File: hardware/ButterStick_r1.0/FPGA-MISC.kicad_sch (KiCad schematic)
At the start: 11 parts, among them U4 ECP5UM5G_85_CABGA381, X1 ASDMB

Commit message: hw.r1d0: Review complete, gerbers generated
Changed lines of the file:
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@@
 (kicad_sch (version 20200618) (host eeschema "5.99.0-unknown-73168a9~101~ubuntu18.04.1")
-  (page 1 18)
+  (page 6 18)
   (paper "A4")
   (title_block
     (title "ButterStick")
-    (date "2020-07-16")
+    (date "2020-07-17")
     (rev "r1.0")
     (company "GsD")
@@
     (stroke (width 0) (type solid) (color 0 0 0 0))
   )
-  (bus (pts (xy 195.58 82.55) (xy 195.58 95.25))
-    (stroke (width 0) (type solid) (color 0 0 0 0))
-  )
-  (bus (pts (xy 195.58 95.25) (xy 195.58 105.41))
-    (stroke (width 0) (type solid) (color 0 0 0 0))
-  )
-  (bus (pts (xy 195.58 105.41) (xy 195.58 110.49))
-    (stroke (width 0) (type solid) (color 0 0 0 0))
-  )
-  (bus (pts (xy 195.58 110.49) (xy 195.58 115.57))
-    (stroke (width 0) (type solid) (color 0 0 0 0))
-  )
+  (bus (pts (xy 195.58 82.55) (xy 195.58 97.79))
+    (stroke (width 0) (type solid) (color 0 0 0 0))
+  )
+  (bus (pts (xy 195.58 97.79) (xy 195.58 107.95))
+    (stroke (width 0) (type solid) (color 0 0 0 0))
+  )
+  (bus (pts (xy 195.58 107.95) (xy 195.58 113.03))
+    (stroke (width 0) (type solid) (color 0 0 0 0))
+  )
+  (bus (pts (xy 195.58 113.03) (xy 195.58 115.57))
+    (stroke (width 0) (type solid) (color 0 0 0 0))
+  )

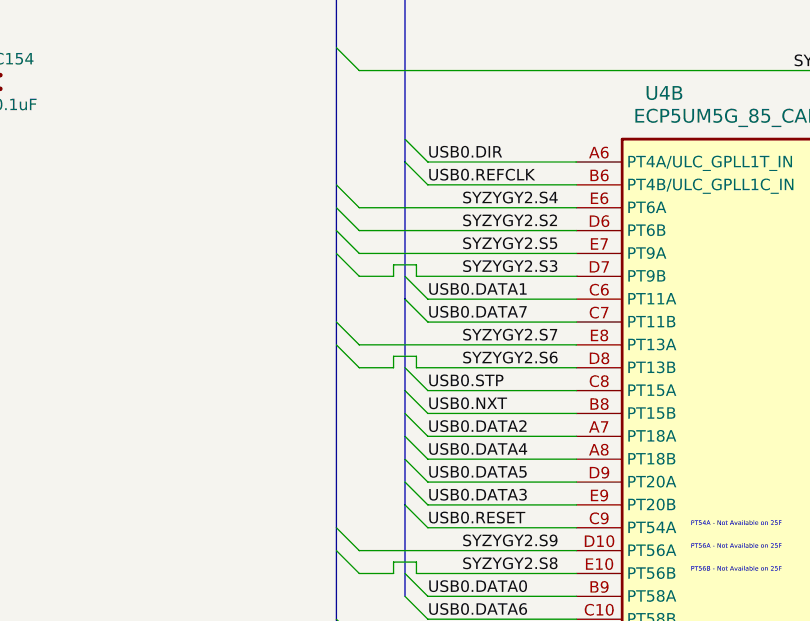
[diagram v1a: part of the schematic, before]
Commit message: hw.r1d0: Update BOM fieids in schematic.
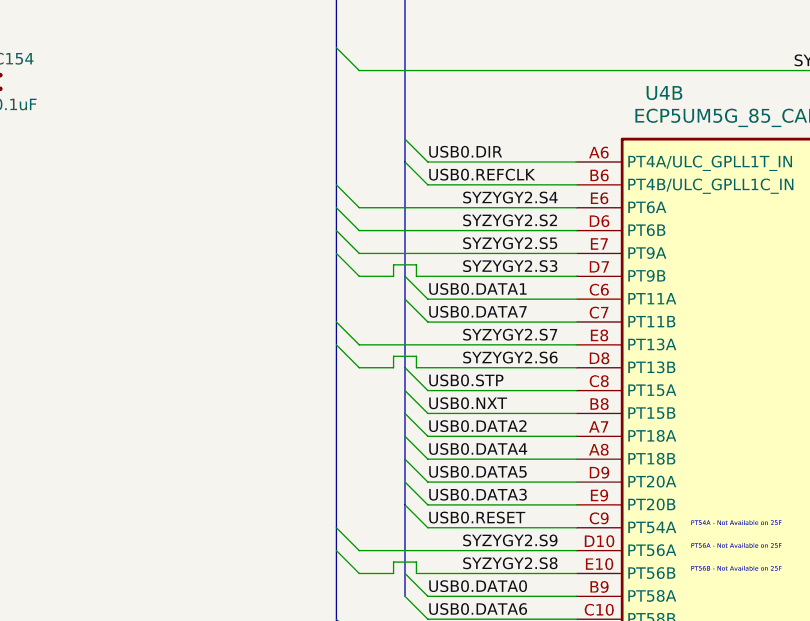
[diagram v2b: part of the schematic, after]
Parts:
- C151, C153, C154, C155, C24: Mfg Samsung Electro-Mechanics -> Yageo; PN CL05B103KP5NNNC -> CC0402KRX5R6BB104; SN-DK 1276-1002-1-ND -> (none); Tol (none) -> 10V / X5R
- C152, C23: Mfg Samsung Electro-Mechanics -> Yageo; PN CL05B104KP5NNNC -> CC0402KRX5R5BB474; SN-DK 1276-1002-1-ND -> (none)
- NT1: PN (none) -> DNP
- R54: Mfg Stackpole Electronics Inc -> Yageo; PN RMCF0402FT20R0 -> RC0402FR-0720RL
- U4: Mfg (none) -> Lattice Semiconductor Corporation; PN (none) -> LFE5UM5G-85F-8BG381C; manf# ECP5UM5G_85 -> (none)
- X1: MFG SiTIME -> (none); Mfg (none) -> ECS Inc.; PN SIT8008BI-72-18N-25.000000G -> ECS-2520SMV-300-FN-TR; SN-DK 1473-30509-1-ND -> (none)
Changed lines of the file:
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@@
     (stroke (width 0) (type solid) (color 0 0 0 0))
   )
-  (bus (pts (xy 195.58 82.55) (xy 195.58 97.79))
+  (bus (pts (xy 195.58 82.55) (xy 195.58 95.25))
     (stroke (width 0) (type solid) (color 0 0 0 0))
   )
-  (bus (pts (xy 195.58 97.79) (xy 195.58 107.95))
+  (bus (pts (xy 195.58 95.25) (xy 195.58 105.41))
     (stroke (width 0) (type solid) (color 0 0 0 0))
   )
-  (bus (pts (xy 195.58 107.95) (xy 195.58 113.03))
+  (bus (pts (xy 195.58 105.41) (xy 195.58 110.49))
     (stroke (width 0) (type solid) (color 0 0 0 0))
   )
-  (bus (pts (xy 195.58 113.03) (xy 195.58 115.57))
+  (bus (pts (xy 195.58 110.49) (xy 195.58 115.57))
     (stroke (width 0) (type solid) (color 0 0 0 0))
   )
@@
       (effects (font (size 1.27 1.27)) hide)
     )
+    (property "PN" "DNP" (id 4) (at 177.8 53.34 0)
+      (effects (font (size 1.27 1.27)) hide)
+    )
   )
   (symbol (lib_id "gkl_power:GND") (at 118.11 44.45 0) (mirror y) (unit 1)
@@
       (effects (font (size 1.27 1.27)) hide)
     )
-    (property "Mfg" "Stackpole Electronics Inc" (id 4) (at 40.64 165.1 0)
-      (effects (font (size 1.27 1.27)) hide)
-    )
-    (property "PN" "RMCF0402FT20R0" (id 5) (at 40.64 165.1 0)
+    (property "Mfg" "Yageo" (id 4) (at 40.64 165.1 0)
+      (effects (font (size 1.27 1.27)) hide)
+    )
+    (property "PN" "RC0402FR-0720RL" (id 5) (at 40.64 165.1 0)
       (effects (font (size 1.27 1.27)) hide)
     )
@@
       (effects (font (size 1.27 1.27)) hide)
     )
-    (property "SN-DK" "1276-1002-1-ND" (id 4) (at -25.4 217.17 0)
-      (effects (font (size 1.27 1.27)) hide)
-    )
-    (property "PN" "CL05B103KP5NNNC" (id 5) (at -25.4 217.17 0)
-      (effects (font (size 1.27 1.27)) hide)
-    )
-    (property "Mfg" "Samsung Electro-Mechanics" (id 6) (at -33.02 215.9 0)
+    (property "SN-DK" "" (id 4) (at -25.4 217.17 0)
+      (effects (font (size 1.27 1.27)) hide)
+    )
+    (property "PN" "CC0402KRX5R6BB104" (id 5) (at -25.4 217.17 0)
+      (effects (font (size 1.27 1.27)) hide)
+    )
+    (property "Mfg" "Yageo" (id 6) (at -33.02 215.9 0)
+      (effects (font (size 1.27 1.27)) hide)
+    )
+    (property "Tol" "10V / X5R" (id 4) (at 124.46 40.64 0)
       (effects (font (size 1.27 1.27)) hide)
     )
@@
       (effects (font (size 1.27 1.27)) hide)
     )
-    (property "SN-DK" "1276-1002-1-ND" (id 4) (at -17.78 250.19 0)
-      (effects (font (size 1.27 1.27)) hide)
-    )
-    (property "PN" "CL05B104KP5NNNC" (id 5) (at -17.78 250.19 0)
-      (effects (font (size 1.27 1.27)) hide)
-    )
-    (property "Mfg" "Samsung Electro-Mechanics" (id 6) (at -15.24 248.92 0)
+    (property "SN-DK" "" (id 4) (at -17.78 250.19 0)
+      (effects (font (size 1.27 1.27)) hide)
+    )
+    (property "PN" "CC0402KRX5R5BB474" (id 5) (at -17.78 250.19 0)
+      (effects (font (size 1.27 1.27)) hide)
+    )
+    (property "Mfg" "Yageo" (id 6) (at -15.24 248.92 0)
       (effects (font (size 1.27 1.27)) hide)
     )
@@
       (effects (font (size 1.27 1.27)) hide)
     )
-    (property "SN-DK" "1276-1002-1-ND" (id 4) (at -8.89 250.19 0)
-      (effects (font (size 1.27 1.27)) hide)
-    )
-    (property "PN" "CL05B103KP5NNNC" (id 5) (at -8.89 250.19 0)
-      (effects (font (size 1.27 1.27)) hide)
-    )
-    (property "Mfg" "Samsung Electro-Mechanics" (id 6) (at -16.51 248.92 0)
+    (property "SN-DK" "" (id 4) (at -8.89 250.19 0)
+      (effects (font (size 1.27 1.27)) hide)
+    )
+    (property "PN" "CC0402KRX5R6BB104" (id 5) (at -8.89 250.19 0)
+      (effects (font (size 1.27 1.27)) hide)
+    )
+    (property "Mfg" "Yageo" (id 6) (at -16.51 248.92 0)
+      (effects (font (size 1.27 1.27)) hide)
+    )
+    (property "Tol" "10V / X5R" (id 4) (at 140.97 73.66 0)
       (effects (font (size 1.27 1.27)) hide)
     )
@@
       (effects (font (size 1.27 1.27)) hide)
     )
-    (property "SN-DK" "1276-1002-1-ND" (id 4) (at -1.27 250.19 0)
-      (effects (font (size 1.27 1.27)) hide)
-    )
-    (property "PN" "CL05B103KP5NNNC" (id 5) (at -1.27 250.19 0)
-      (effects (font (size 1.27 1.27)) hide)
-    )
-    (property "Mfg" "Samsung Electro-Mechanics" (id 6) (at -8.89 248.92 0)
+    (property "SN-DK" "" (id 4) (at -1.27 250.19 0)
+      (effects (font (size 1.27 1.27)) hide)
+    )
+    (property "PN" "CC0402KRX5R6BB104" (id 5) (at -1.27 250.19 0)
+      (effects (font (size 1.27 1.27)) hide)
+    )
+    (property "Mfg" "Yageo" (id 6) (at -8.89 248.92 0)
+      (effects (font (size 1.27 1.27)) hide)
+    )
+    (property "Tol" "10V / X5R" (id 4) (at 148.59 73.66 0)
       (effects (font (size 1.27 1.27)) hide)
     )
@@
       (effects (font (size 1.27 1.27)) hide)
     )
-    (property "SN-DK" "1276-1002-1-ND" (id 4) (at 111.76 260.35 0)
-      (effects (font (size 1.27 1.27)) hide)
-    )
-    (property "PN" "CL05B104KP5NNNC" (id 5) (at 111.76 260.35 0)
-      (effects (font (size 1.27 1.27)) hide)
-    )
-    (property "Mfg" "Samsung Electro-Mechanics" (id 6) (at 114.3 259.08 0)
+    (property "SN-DK" "" (id 4) (at 111.76 260.35 0)
+      (effects (font (size 1.27 1.27)) hide)
+    )
+    (property "PN" "CC0402KRX5R5BB474" (id 5) (at 111.76 260.35 0)
+      (effects (font (size 1.27 1.27)) hide)
+    )
+    (property "Mfg" "Yageo" (id 6) (at 114.3 259.08 0)
       (effects (font (size 1.27 1.27)) hide)
     )
@@
       (effects (font (size 1.27 1.27)) hide)
     )
-    (property "SN-DK" "1276-1002-1-ND" (id 4) (at 120.65 260.35 0)
-      (effects (font (size 1.27 1.27)) hide)
-    )
-    (property "PN" "CL05B103KP5NNNC" (id 5) (at 120.65 260.35 0)
-      (effects (font (size 1.27 1.27)) hide)
-    )
-    (property "Mfg" "Samsung Electro-Mechanics" (id 6) (at 113.03 259.08 0)
+    (property "SN-DK" "" (id 4) (at 120.65 260.35 0)
+      (effects (font (size 1.27 1.27)) hide)
+    )
+    (property "PN" "CC0402KRX5R6BB104" (id 5) (at 120.65 260.35 0)
+      (effects (font (size 1.27 1.27)) hide)
+    )
+    (property "Mfg" "Yageo" (id 6) (at 113.03 259.08 0)
+      (effects (font (size 1.27 1.27)) hide)
+    )
+    (property "Tol" "10V / X5R" (id 4) (at 270.51 83.82 0)
       (effects (font (size 1.27 1.27)) hide)
     )
@@
       (effects (font (size 1.27 1.27)) hide)
     )
-    (property "SN-DK" "1276-1002-1-ND" (id 4) (at 128.27 260.35 0)
-      (effects (font (size 1.27 1.27)) hide)
-    )
-    (property "PN" "CL05B103KP5NNNC" (id 5) (at 128.27 260.35 0)
-      (effects (font (size 1.27 1.27)) hide)
-    )
-    (property "Mfg" "Samsung Electro-Mechanics" (id 6) (at 120.65 259.08 0)
+    (property "SN-DK" "" (id 4) (at 128.27 260.35 0)
+      (effects (font (size 1.27 1.27)) hide)
+    )
+    (property "PN" "CC0402KRX5R6BB104" (id 5) (at 128.27 260.35 0)
+      (effects (font (size 1.27 1.27)) hide)
+    )
+    (property "Mfg" "Yageo" (id 6) (at 120.65 259.08 0)
+      (effects (font (size 1.27 1.27)) hide)
+    )
+    (property "Tol" "10V / X5R" (id 4) (at 278.13 83.82 0)
       (effects (font (size 1.27 1.27)) hide)
     )
@@
       (effects (font (size 1.27 1.27)) hide)
     )
-    (property "SN-DK" " 1473-30509-1-ND " (id 4) (at 320.04 189.23 0)
-      (effects (font (size 1.27 1.27)) hide)
-    )
-    (property "PN" "SIT8008BI-72-18N-25.000000G" (id 5) (at 320.04 189.23 0)
-      (effects (font (size 1.27 1.27)) hide)
-    )
-    (property "MFG" "SiTIME" (id 6) (at 243.84 193.04 0)
+    (property "SN-DK" "" (id 4) (at 320.04 189.23 0)
+      (effects (font (size 1.27 1.27)) hide)
+    )
+    (property "PN" "ECS-2520SMV-300-FN-TR" (id 5) (at 320.04 189.23 0)
+      (effects (font (size 1.27 1.27)) hide)
+    )
+    (property "MFG" "" (id 6) (at 243.84 193.04 0)
+      (effects (font (size 1.27 1.27)) hide)
+    )
+    (property "Mfg" "ECS Inc." (id 4) (at 106.68 40.64 0)
       (effects (font (size 1.27 1.27)) hide)
     )
@@
       (effects (font (size 1.524 1.524)) (justify right) hide)
     )
-    (property "manf#" "ECP5UM5G_85" (id 4) (at 218.44 83.82 0)
+    (property "manf#" "" (id 4) (at 218.44 83.82 0)
       (effects (font (size 1.524 1.524)) (justify right) hide)
+    )
+    (property "Mfg" "Lattice Semiconductor Corporation" (id 4) (at 214.63 82.55 0)
+      (effects (font (size 1.27 1.27)) hide)
+    )
+    (property "PN" "LFE5UM5G-85F-8BG381C" (id 5) (at 214.63 82.55 0)
+      (effects (font (size 1.27 1.27)) hide)
     )
   )
@@
       (effects (font (size 1.524 1.524)) (justify right) hide)
     )
-    (property "manf#" "ECP5UM5G_85" (id 4) (at 90.17 72.39 0)
+    (property "manf#" "" (id 4) (at 90.17 72.39 0)
       (effects (font (size 1.524 1.524)) (justify right) hide)
     )
-  )
+    (property "Mfg" "Lattice Semiconductor Corporation" (id 4) (at 86.36 71.12 0)
+      (effects (font (size 1.27 1.27)) hide)
+    )
+    (property "PN" "LFE5UM5G-85F-8BG381C" (id 5) (at 86.36 71.12 0)
+      (effects (font (size 1.27 1.27)) hide)
+    )
+  )

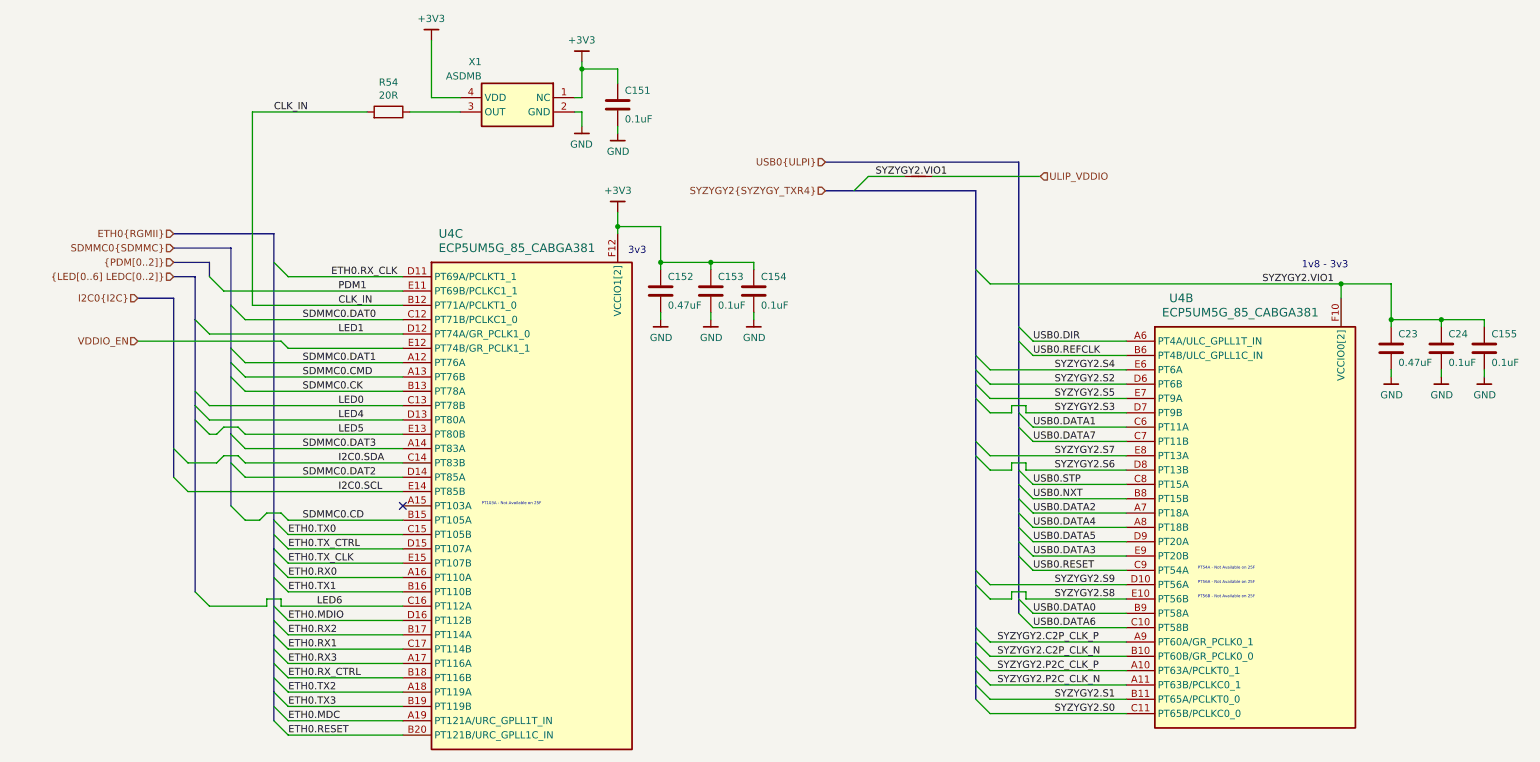
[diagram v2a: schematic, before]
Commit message: hw.r1d0: Fix RGMII straps
This commit correctly sets the stop resistos on the RGMII lines to 1K5
instead of DNP.
Also regenerate and add a schematic in PDF format.

Fixes #6
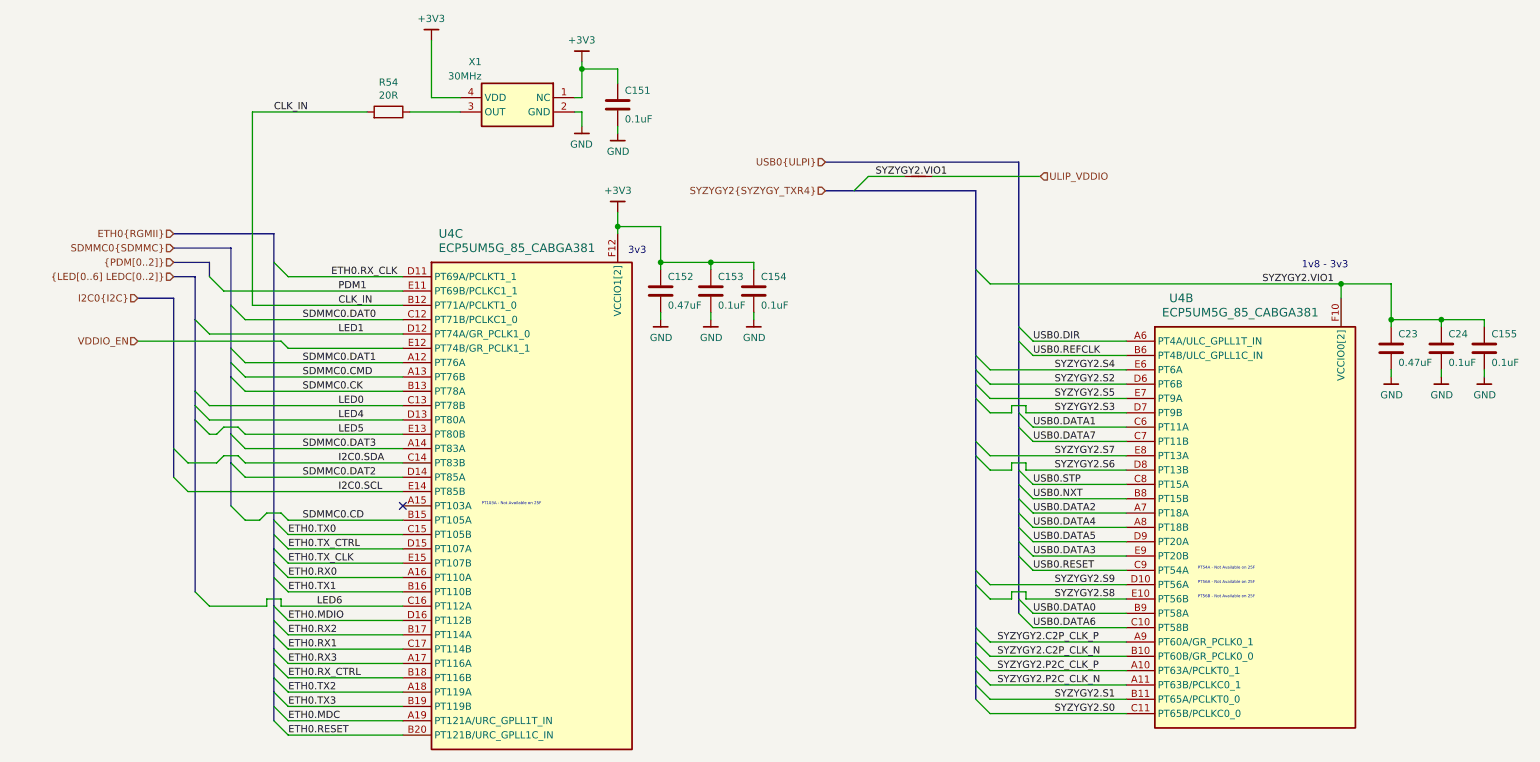
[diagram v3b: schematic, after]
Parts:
- U4: PN LFE5UM5G-85F-8BG381C -> LFE5UM5G-85F-8BG381I
- X1: value ASDMB -> 30MHz
